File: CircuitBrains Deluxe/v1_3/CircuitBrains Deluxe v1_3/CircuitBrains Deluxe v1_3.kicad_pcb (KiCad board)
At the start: 2 copper layers, 29 x 29 mm, 31 parts, among them SW1 KMR231, U1 S25FL064LABNFI040, U2 AP2112K-3.3, U3 ATSAMD51J19A-MU, U4 48SOM, Y1 FC-135 32.7680KA-A5

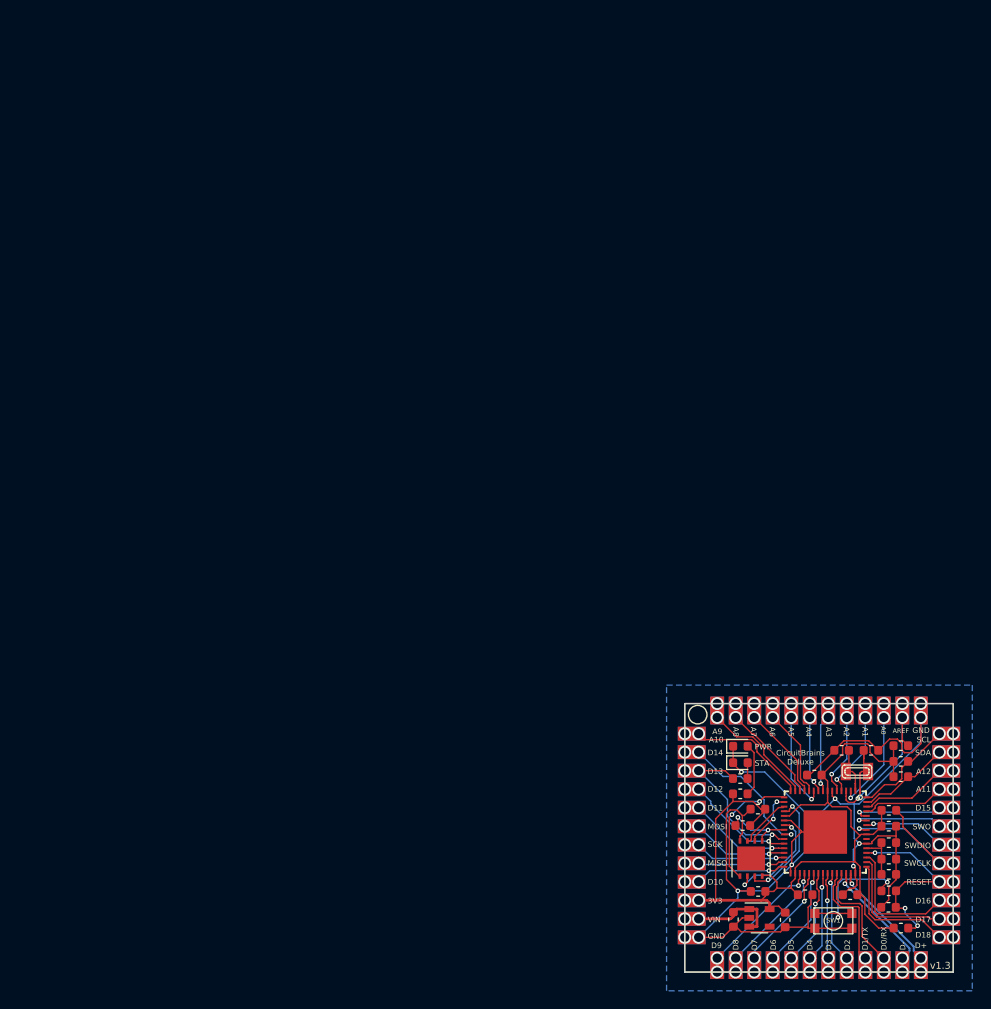
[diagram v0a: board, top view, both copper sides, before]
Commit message: Fixed silk label size on board
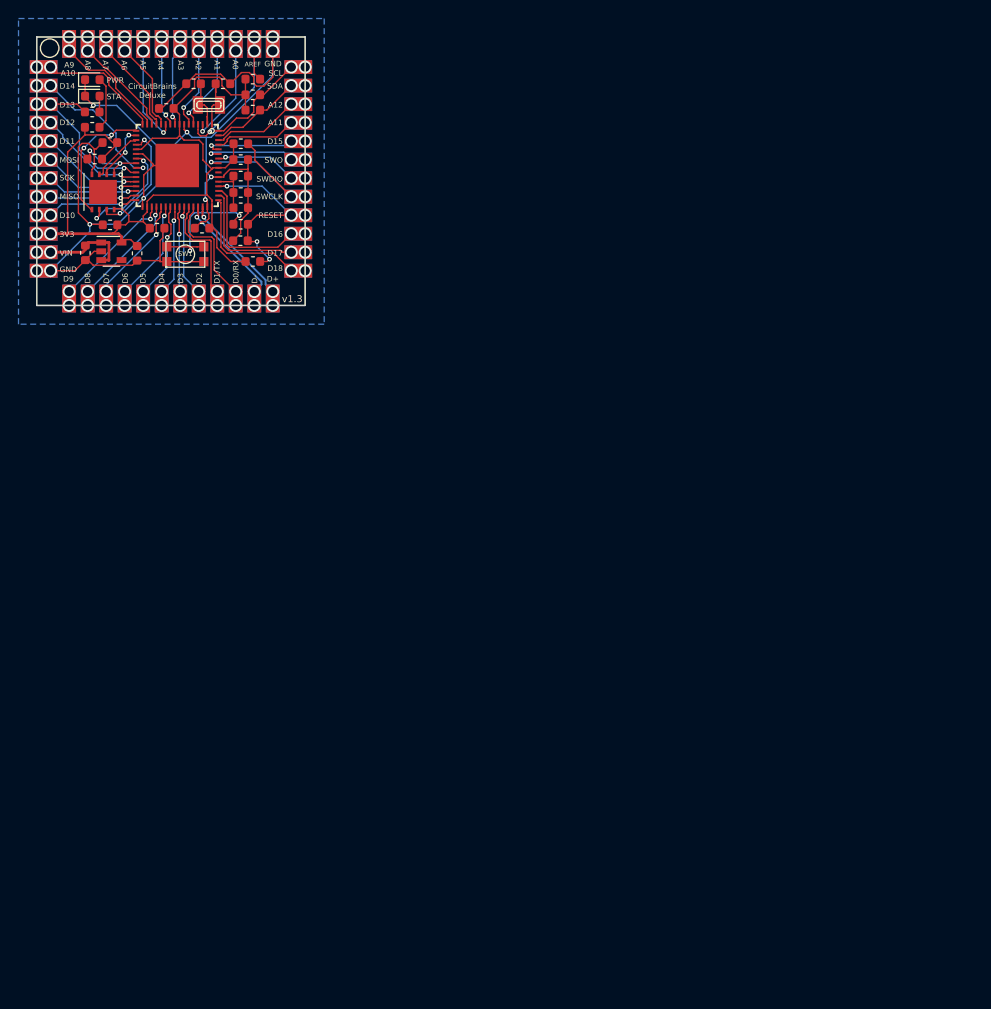
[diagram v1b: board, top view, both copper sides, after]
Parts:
- U1: footprint Package_SON:WSON-8_4x4mm_P0.8mm -> Kevin-SON:WSON-8_4x4mm_P0.8mm
- moved C1 100.4 mm to (32.1, 19.5)
- moved C10 100.4 mm to (29.1, 22.2)
- moved C11 100.4 mm to (23.0, 25.9)
- moved C12 100.4 mm to (33.0, 35.1)
- moved C13 100.4 mm to (28.2, 35.1)
- moved C14 100.4 mm to (37.2, 27.7)
- moved C2 100.4 mm to (35.3, 19.5)
- moved C3 100.4 mm to (37.2, 36.5)
- moved C4 100.4 mm to (20.4, 37.8)
- moved C5 100.4 mm to (23.1, 34.7)
- moved C6 100.4 mm to (37.2, 32.9)
- moved C7 100.4 mm to (26.0, 37.8)
- moved C8 100.4 mm to (37.2, 31.3)
- moved C9 100.4 mm to (37.2, 29.5)
- moved LED1 100.4 mm to (21.2, 19.1)
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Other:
- board text added: "@NullByteLabs"
- board text removed: "@kevinneubauer"
